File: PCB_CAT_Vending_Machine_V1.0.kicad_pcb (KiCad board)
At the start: 2 copper layers, 108 x 129 mm, 221 parts, among them J1 12Vin, J10 Load_0, J11 Load_1, J12 Load_2, J13 Load_3, J14 Load_4, J15 Load_5, J16 Load_6, J17 Load_07, J18 Screen, J19 Banknote, J2 Button_0, J20 QR ESP32, J21 Coin, J22 RASPI, J23 Water Level, J3 Button_1, J4 Button_2, J5 Button_3, J6 Button_4, J7 Button_5, J8 Button_6, J9 Button_7, Q1 2N7002, Q12 AO3400A, Q13 AO3400A, Q14 AO3400A, Q15 AO3400A, Q16 AO3400A, Q17 AO3400A, Q18 AO3400A, Q2 2N7002, Q3 AO3400A, Q4 2N7002, Q5 2N7002, Q6 2N7002, Q7 2N7002, Q8 2N7002, Q9 2N7002, SW1 Pairing, SW2 Add 10 BTH, U1 ESP32-S3-N16R8-Module, U10 PC817C-S, U11 PC817C-S, U12 PC817C-S, U13 PCA9557PW, U2 PCA9557PW, U3 PCA9557PW, U4 TPS5430DDA, U5 PC817C-S, U6 PC817C-S, U7 PC817C-S, U8 PC817C-S, U9 PC817C-S

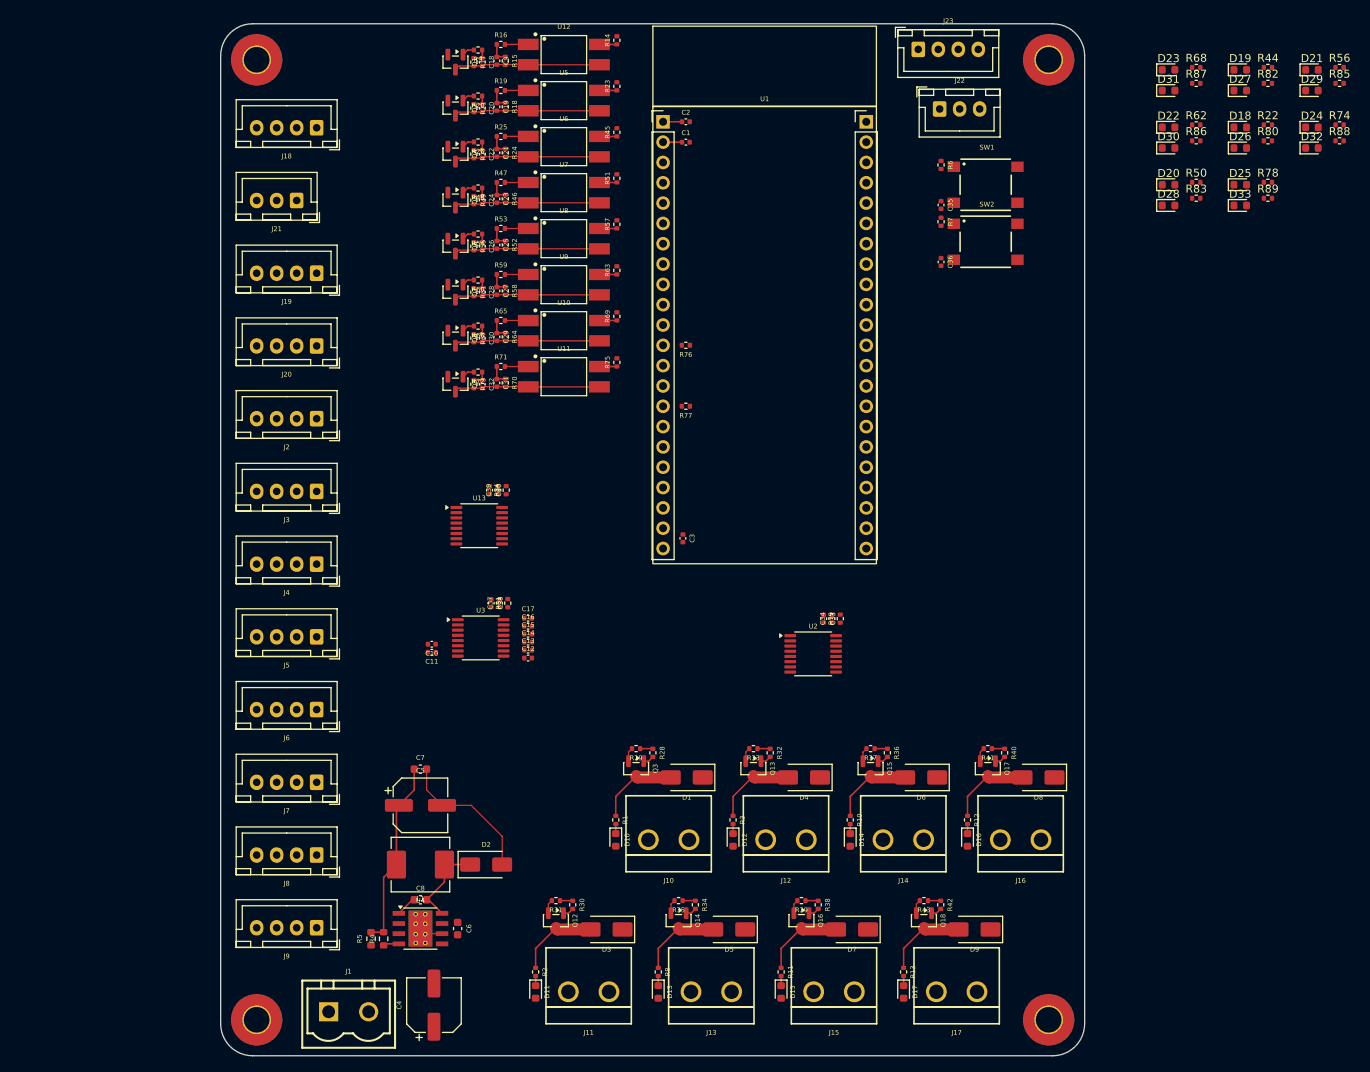
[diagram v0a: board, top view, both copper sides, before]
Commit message: PCB Connector Position
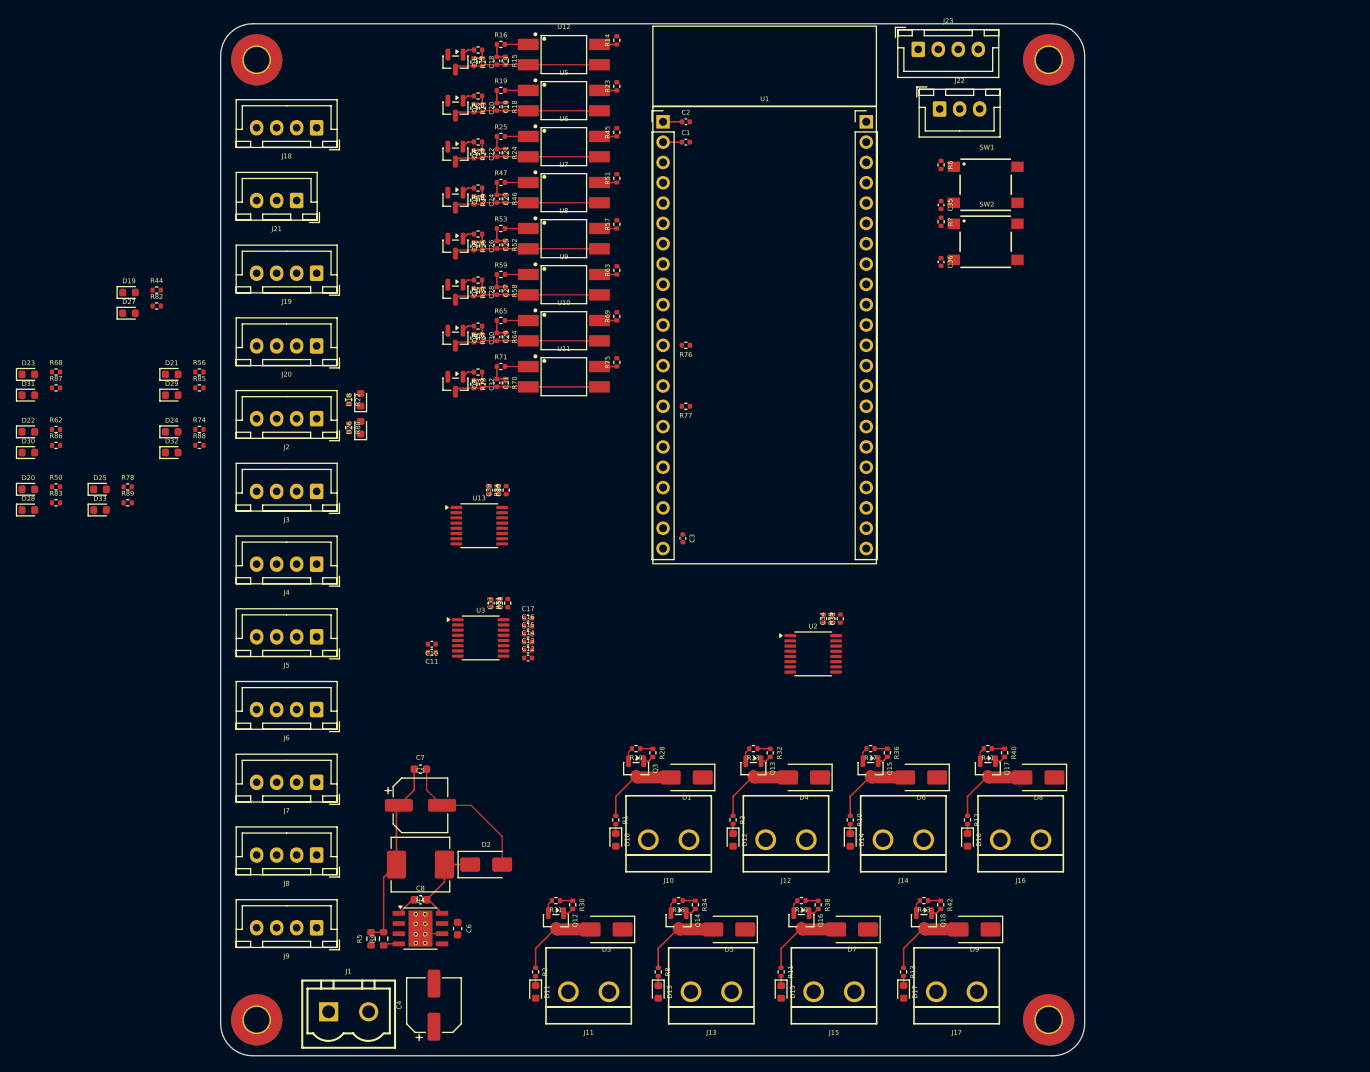
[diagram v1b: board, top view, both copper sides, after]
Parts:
- moved D20 147.5 mm to (-4.04, 78.2)
- moved D21 147.5 mm to (13.9, 63.8)
- moved D22 147.5 mm to (-4.04, 71.0)
- moved D23 147.5 mm to (-4.04, 63.8)
- moved D24 147.5 mm to (13.9, 71.0)
- moved D28 147.5 mm to (-4.04, 80.8)
- moved D29 147.5 mm to (13.9, 66.4)
- moved D30 147.5 mm to (-4.04, 73.6)
- moved D31 147.5 mm to (-4.04, 66.4)
- moved D32 147.5 mm to (13.9, 73.6)
- moved R56 147.5 mm to (17.3, 63.5)
- moved R74 147.5 mm to (17.3, 70.7)
- moved R78 147.5 mm to (8.38, 77.9)
- moved R85 147.5 mm to (17.3, 65.5)
- moved R88 147.5 mm to (17.3, 72.7)
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
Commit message: led
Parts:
- moved D27 39.2 mm to (39.5, 80.2), turned to 90 degrees
- moved D19 38.8 mm to (39.6, 76.9), turned to 90 degrees
- moved R82 35.2 mm to (36.9, 80.1), turned to -90 degrees
- moved R44 34.0 mm to (36.7, 76.6), turned to -90 degrees

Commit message: 3d
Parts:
- added J24: Water Level, Connector_JST:JST_XH_B4B-XH-A_1x04_P2.50mm_Vertical, F.Cu at (122.1, 56.9)
- added J25: Water Level, Connector_JST:JST_XH_B4B-XH-A_1x04_P2.50mm_Vertical, F.Cu at (122.1, 64.7)
- added J26: Water Level, Connector_JST:JST_XH_B4B-XH-A_1x04_P2.50mm_Vertical, F.Cu at (122.1, 72.5)
- added J27: Water Level, Connector_JST:JST_XH_B4B-XH-A_1x04_P2.50mm_Vertical, F.Cu at (122.1, 80.2)
- added J28: Water Level, Connector_JST:JST_XH_B4B-XH-A_1x04_P2.50mm_Vertical, F.Cu at (122.1, 88.0)
- moved R87 63.9 mm to (41.0, 114.0)
- moved D23 63.9 mm to (37.5, 112.3)
- moved D31 63.9 mm to (37.5, 114.9)
- moved R68 63.9 mm to (41.0, 112.0)
- moved D25 62.4 mm to (37.4, 131.5)
- moved D33 62.4 mm to (37.4, 134.1)
- moved R89 62.4 mm to (40.9, 133.2)
- moved R78 62.4 mm to (40.9, 131.2)
- moved R74 57.2 mm to (41.9, 122.4)
- moved D24 57.2 mm to (38.4, 122.7)
- moved D32 57.2 mm to (38.4, 125.3)
- moved R88 57.2 mm to (41.9, 124.4)
- moved D30 53.8 mm to (38.4, 106.6)
- moved R62 53.8 mm to (41.9, 103.7)
- moved D22 53.8 mm to (38.4, 104.0)
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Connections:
- net /Microcontroller/Water_Level.Echo renamed /Peripheral/Water_Trigger0
- J23 pad 1: +5V -> unconnected-(J23-Pin_1-Pad1)
- J23 pad 2: /Microcontroller/Water_Level.Trig -> GND
- J23 pad 4: GND -> +12V

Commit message: SCH finish
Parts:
- added C41: 100nF, Capacitor_SMD:C_0402_1005Metric, F.Cu at (95.4, 95.0)
- added C42: 100nF, Capacitor_SMD:C_0402_1005Metric, F.Cu at (94.4, 95.1)
- added C43: 1nF, Capacitor_SMD:C_0402_1005Metric, F.Cu at (71.9, 109.5)
- added C44: 1nF, Capacitor_SMD:C_0402_1005Metric, F.Cu at (61.9, 128.5)
- added C45: 1nF, Capacitor_SMD:C_0402_1005Metric, F.Cu at (86.6, 109.5)
- added C46: 1nF, Capacitor_SMD:C_0402_1005Metric, F.Cu at (77.2, 128.4)
- added C47: 1nF, Capacitor_SMD:C_0402_1005Metric, F.Cu at (101.2, 109.4)
- added C48: 1nF, Capacitor_SMD:C_0402_1005Metric, F.Cu at (92.6, 128.4)
- added C49: 1nF, Capacitor_SMD:C_0402_1005Metric, F.Cu at (115.9, 109.5)
- added C50: 1nF, Capacitor_SMD:C_0402_1005Metric, F.Cu at (107.9, 128.5)
- added J29: QR_Button, Connector_JST:JST_XH_B5B-XH-A_1x05_P2.50mm_Vertical, F.Cu at (42.1, 24.8)
- added Q10: PT15-21C/TR8, LED_SMD:LED_1206_3216Metric, F.Cu at (69.0, 95.6)
- added R90: 10k, Resistor_SMD:R_0402_1005Metric, F.Cu at (96.5, 95.0)
- added R91: 10k, Resistor_SMD:R_0402_1005Metric, F.Cu at (74.7, 95.8)
- added U14: PCA9557PW, Package_SO:TSSOP-16_4.4x5mm_P0.65mm, F.Cu at (92.2, 99.7)
- R1, R10, R11, R12, R13, R2, R22, R3, R44, R50, R56, R62, R68, R74, R78, R8, R80, R82, R83, R85, R86, R87, R88, R89: value 4.7k -> 3k
- moved J23 33.2 mm to (123.6, 52.1), turned to 180 degrees
- moved C36 14.5 mm to (108.3, 35.4)
- moved R7 14.5 mm to (108.3, 30.4)
- moved SW1 14.5 mm to (113.9, 25.8)
- moved SW2 14.5 mm to (113.9, 32.9)
- moved C35 14.5 mm to (108.3, 28.3)
- moved R6 14.5 mm to (108.3, 23.3)
- moved J22 14.4 mm to (118.6, 42.1)
- moved R79 11.1 mm to (86.4, 95.1)
- moved U2 11.1 mm to (83.0, 99.5)
- moved C33 11.1 mm to (84.4, 95.1)
- moved C34 11.1 mm to (85.4, 95.1)
- moved J28 8.71 mm to (123.6, 96.6)
- moved J27 7.62 mm to (123.6, 87.7)
- moved J26 6.53 mm to (123.6, 78.8)
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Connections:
- J23 pad 3: /Peripheral/Water_Trigger0 -> /Microcontroller/Water_Trigger0
- J24 pad 3: /Peripheral/Water_Trigger1 -> /Microcontroller/Water_Trigger1
- J25 pad 3: /Peripheral/Water_Trigger2 -> /Microcontroller/Water_Trigger2
- J26 pad 3: /Peripheral/Water_Trigger3 -> /Microcontroller/Water_Trigger3
- J27 pad 3: /Peripheral/Water_Trigger4 -> /Microcontroller/Water_Trigger4
- J28 pad 3: /Peripheral/Water_Trigger5 -> /Microcontroller/Water_Trigger5
- Q1 pad 2: /Connector/BTN0/GND_LED0 -> GND
- Q1 pad 3: GND -> /Connector/BTN0/GND_LED0
- Q2 pad 2: /Connector/BTN1/GND_LED1 -> GND
- Q2 pad 3: GND -> /Connector/BTN1/GND_LED1
- Q4 pad 2: /Connector/BTN2/GND_LED2 -> GND
- Q4 pad 3: GND -> /Connector/BTN2/GND_LED2
- Q5 pad 2: /Connector/BTN3/GND_LED3 -> GND
- Q5 pad 3: GND -> /Connector/BTN3/GND_LED3
- Q6 pad 2: /Connector/BTN4/GND_LED4 -> GND
- Q6 pad 3: GND -> /Connector/BTN4/GND_LED4
- Q7 pad 2: /Connector/BTN5/GND_LED5 -> GND
- Q7 pad 3: GND -> /Connector/BTN5/GND_LED5
- Q8 pad 2: /Connector/BTN6/GND_LED6 -> GND
- Q8 pad 3: GND -> /Connector/BTN6/GND_LED6
- Q9 pad 2: /Connector/BTN7/GND_LED7 -> GND
- Q9 pad 3: GND -> /Connector/BTN7/GND_LED7
- U1 pad 37: unconnected-(U1-GPIO40-Pad37) -> /Microcontroller/QR_Button0
- U1 pad 38: unconnected-(U1-GPIO41-Pad38) -> /Microcontroller/QR_Button1
- U1 pad 39: unconnected-(U1-GPIO42-Pad39) -> /Microcontroller/QR_Button2
- U1 pad 40: /Microcontroller/SW2 -> unconnected-(U1-GPIO2-Pad40)
- U1 pad 41: /Microcontroller/SW1 -> /Microcontroller/LightSen
- U3 pad 4: GND -> +3.3V
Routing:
- net GND: track 181.0 -> 152.7 mm

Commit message: finish no review
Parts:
- added C51: 10nF, Capacitor_SMD:C_0402_1005Metric, F.Cu at (105.0, 45.5)
- added C52: 10nF, Capacitor_SMD:C_0402_1005Metric, F.Cu at (105.0, 48.0)
- added C53: 10nF, Capacitor_SMD:C_0402_1005Metric, F.Cu at (105.0, 50.5)
- added J30: DoorSensor, Connector_JST:JST_XH_B2B-XH-A_1x02_P2.50mm_Vertical, F.Cu at (123.6, 33.0)
- added R92: 10k, Resistor_SMD:R_0402_1005Metric, F.Cu at (104.0, 45.5)
- added R93: 10k, Resistor_SMD:R_0402_1005Metric, F.Cu at (104.0, 48.0)
- added R94: 10k, Resistor_SMD:R_0402_1005Metric, F.Cu at (104.0, 50.5)
- added R95: 10k, Resistor_SMD:R_0402_1005Metric, F.Cu at (108.9, 51.5)
- added R96: 100, Resistor_SMD:R_0402_1005Metric, F.Cu at (104.5, 52.6)
- J29: footprint Connector_JST:JST_XH_B5B-XH-A_1x05_P2.50mm_Vertical -> Connector_JST:JST_XH_B4B-XH-A_1x04_P2.50mm_Vertical
- moved J29 83.3 mm to (123.6, 42.1)
- moved J22 76.2 mm to (44.5, 24.3), turned to 180 degrees
- moved SW1 75.0 mm to (100.3, 99.5), turned to -90 degrees
- moved R91 73.5 mm to (56.7, 24.5), turned to 180 degrees
- moved Q10 71.6 mm to (60.0, 24.5)
- moved R6 70.9 mm to (102.8, 94.0), turned to 180 degrees
- moved SW2 66.9 mm to (107.5, 99.5), turned to -90 degrees
- moved C35 66.5 mm to (97.8, 94.0), turned to 180 degrees
- moved R7 63.6 mm to (110.0, 94.0), turned to 180 degrees
- moved C36 58.6 mm to (105.0, 94.0), turned to 180 degrees
- moved C15 54.5 mm to (59.9, 41.9)
- moved C14 54.5 mm to (59.9, 42.8)
- moved C13 54.5 mm to (59.9, 43.8)
- moved C12 54.5 mm to (59.9, 44.8)
- moved C11 54.4 mm to (59.9, 45.8), turned to 0 degrees
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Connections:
- J1 pad 1: +12V -> GND
- J1 pad 2: GND -> +12V
- J18 pad 1: +3.3V -> /Microcontroller/Screen.CLK
- J18 pad 2: GND -> /Microcontroller/Screen.DIO
- J18 pad 3: /Microcontroller/Screen.DIO -> GND
- J18 pad 4: /Microcontroller/Screen.CLK -> +3.3V
- J19 pad 1: +12V -> GND
- J19 pad 2: GND -> /Microcontroller/Pulse
- J19 pad 3: /Microcontroller/Pulse -> GND
- J19 pad 4: GND -> +12V
- J20 pad 1: +5V -> GND
- J20 pad 4: GND -> +5V
- J21 pad 1: +12V -> GND
- J21 pad 3: GND -> +12V
- J29 pad 2: /Peripheral/QR_Button0 -> /Microcontroller/QR_Button0
- J29 pad 3: /Peripheral/QR_Button1 -> /Microcontroller/QR_Button1
- J29 pad 4: /Peripheral/QR_Button2 -> /Microcontroller/QR_Button2
- U1 pad 17: /Microcontroller/COIN -> /Microcontroller/Pulse
- U1 pad 18: /Microcontroller/Pulse -> /Microcontroller/COIN
- U1 pad 36: unconnected-(U1-GPIO39-Pad36) -> /Microcontroller/Door
- U13 pad 10: /Connector/LED3 -> /Connector/LED4
- U13 pad 11: /Connector/LED4 -> /Connector/LED3
- U13 pad 12: /Connector/LED5 -> /Connector/LED2
- U13 pad 13: /Connector/LED6 -> /Connector/LED1
- U13 pad 14: /Connector/LED7 -> /Connector/LED0
- U13 pad 6: /Connector/LED0 -> /Connector/LED7
- U13 pad 7: /Connector/LED1 -> /Connector/LED6
- U13 pad 9: /Connector/LED2 -> /Connector/LED5
- U14 pad 10: /Microcontroller/Water_Trigger3 -> /Microcontroller/Water_Trigger2
- U14 pad 11: /Microcontroller/Water_Trigger4 -> /Microcontroller/Water_Trigger1
- U14 pad 12: /Microcontroller/Water_Trigger5 -> /Microcontroller/Water_Trigger0
- U14 pad 6: /Microcontroller/Water_Trigger0 -> /Microcontroller/Water_Trigger4
- U14 pad 7: /Microcontroller/Water_Trigger1 -> /Microcontroller/Water_Trigger5
- U14 pad 9: /Microcontroller/Water_Trigger2 -> /Microcontroller/Water_Trigger3
- U2 pad 10: /Connector/LD3 -> /Connector/LD2
- U2 pad 11: /Connector/LD4 -> /Connector/LD5
- U2 pad 12: /Connector/LD5 -> /Connector/LD4
- U2 pad 13: /Connector/LD6 -> /Connector/LD7
- U2 pad 14: /Connector/LD7 -> /Connector/LD6
- U2 pad 9: /Connector/LD2 -> /Connector/LD3
- U3 pad 10: /Connector/BTN3 -> /Connector/BTN1
- U3 pad 11: /Connector/BTN4 -> /Connector/BTN2
- U3 pad 12: /Connector/BTN5 -> /Connector/BTN3
- U3 pad 13: /Connector/BTN6 -> /Connector/BTN4
- U3 pad 14: /Connector/BTN7 -> /Connector/BTN5
- U3 pad 6: /Connector/BTN0 -> /Connector/BTN7
- U3 pad 7: /Connector/BTN1 -> /Connector/BTN6
- U3 pad 9: /Connector/BTN2 -> /Connector/BTN0
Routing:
- net +12V: track 0.00 -> 1004.4 mm, vias 0 -> 49
- net +3.3V: track 4.74 -> 603.1 mm, vias 0 -> 23
- net /Microcontroller/I2C_SDA: track 0.00 -> 206.0 mm, vias 0 -> 3
- net /Microcontroller/I2C_SCL: track 0.00 -> 202.1 mm, vias 0 -> 3
- net +5V: track 23.5 -> 197.8 mm, vias 0 -> 9
- net /Microcontroller/RASPI.RX: track 0.00 -> 137.5 mm
- net /Microcontroller/RASPI.TX: track 0.00 -> 136.8 mm
- net GND: track 152.7 -> 289.0 mm, vias 0 -> 324
- net /Microcontroller/COIN: track 0.00 -> 100.0 mm
- net /Connector/LED7: track 2.12 -> 91.1 mm, vias 0 -> 2
- net /Microcontroller/Pulse: track 0.00 -> 88.2 mm
- net /Connector/LED5: track 2.12 -> 84.5 mm, vias 0 -> 2
- net /Connector/LED6: track 2.12 -> 83.0 mm, vias 0 -> 2
- net /Connector/LED4: track 2.12 -> 77.9 mm, vias 0 -> 2
- net /Connector/LED3: track 2.12 -> 71.4 mm, vias 0 -> 2
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- added copper zone on B.Cu, net +12V
- added copper zone on F.Cu, net +12V
- added copper zone on F.Cu, net +5V
- added copper zone on B.Cu, net GND
- added copper zone on F.Cu, net GND
- added copper zone on F.Cu, net Net-(D2-K)

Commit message: success
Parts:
- removed R80, R82, R83, R85, R86, R87, R88, R89: 3k, Resistor_SMD:R_0402_1005Metric
- added C54: 10nF, Capacitor_SMD:C_0402_1005Metric, F.Cu at (104.5, 39.9)
- added C55: 100nF, Capacitor_SMD:C_0402_1005Metric, F.Cu at (105.0, 53.0)
- added C57: 10nF, Capacitor_SMD:C_0402_1005Metric, F.Cu at (91.6, 99.5)
- added C58: 10nF, Capacitor_SMD:C_0402_1005Metric, F.Cu at (91.6, 101.3)
- added C59: 10nF, Capacitor_SMD:C_0402_1005Metric, F.Cu at (90.5, 91.3)
- added C60: 10nF, Capacitor_SMD:C_0402_1005Metric, F.Cu at (88.6, 91.3)
- added C61: 10nF, Capacitor_SMD:C_0402_1005Metric, F.Cu at (86.7, 91.3)
- added C62: 10nF, Capacitor_SMD:C_0402_1005Metric, F.Cu at (84.8, 91.3)
- added JP1: Bankenote Selector, Jumper:SolderJumper-3_P1.3mm_Open_RoundedPad1.0x1.5mm, F.Cu at (65.0, 39.0)
- added R100: 10k, Resistor_SMD:R_0402_1005Metric, F.Cu at (90.5, 90.3)
- added R101: 10k, Resistor_SMD:R_0402_1005Metric, F.Cu at (88.6, 90.3)
- added R102: 10k, Resistor_SMD:R_0402_1005Metric, F.Cu at (86.7, 90.3)
- added R103: 10k, Resistor_SMD:R_0402_1005Metric, F.Cu at (84.8, 90.3)
- added R104: 27k, Resistor_SMD:R_0603_1608Metric, F.Cu at (117.8, 91.5)
- added R105: 27k, Resistor_SMD:R_0603_1608Metric, F.Cu at (117.8, 100.4)
- added R106: 27k, Resistor_SMD:R_0603_1608Metric, F.Cu at (117.8, 82.6)
- added R107: 27k, Resistor_SMD:R_0603_1608Metric, F.Cu at (117.8, 73.7)
- added R108: 27k, Resistor_SMD:R_0603_1608Metric, F.Cu at (117.8, 64.8)
- added R109: 27k, Resistor_SMD:R_0603_1608Metric, F.Cu at (117.8, 55.9)
- added R110: 220, Resistor_SMD:R_0402_1005Metric, F.Cu at (90.2, 100.9)
- added R111: 220, Resistor_SMD:R_0402_1005Metric, F.Cu at (89.2, 93.4)
- added R112: 220, Resistor_SMD:R_0402_1005Metric, F.Cu at (88.2, 93.4)
- added R113: 220, Resistor_SMD:R_0402_1005Metric, F.Cu at (87.1, 93.4)
- added R114: 220, Resistor_SMD:R_0402_1005Metric, F.Cu at (86.1, 93.4)
- added R115: 4.7k, Resistor_SMD:R_0402_1005Metric, F.Cu at (78.2, 39.9)
- added R116: 4.7k, Resistor_SMD:R_0402_1005Metric, F.Cu at (78.2, 42.4)
- added R117: 10k, Resistor_SMD:R_0402_1005Metric, F.Cu at (69.5, 107.8)
- added R118: 10k, Resistor_SMD:R_0402_1005Metric, F.Cu at (85.9, 107.8)
- added R119: 10k, Resistor_SMD:R_0402_1005Metric, F.Cu at (81.5, 108.5)
- added R120: 10k, Resistor_SMD:R_0402_1005Metric, F.Cu at (99.3, 106.5)
- added R121: 10k, Resistor_SMD:R_0402_1005Metric, F.Cu at (94.8, 107.2)
- added R122: 10k, Resistor_SMD:R_0402_1005Metric, F.Cu at (82.5, 104.7)
- added R123: 4.7k, Resistor_SMD:R_0402_1005Metric, F.Cu at (78.2, 75.5)
- added R124: 10k, Resistor_SMD:R_0402_1005Metric, F.Cu at (101.8, 106.4)
- added R97: 220, Resistor_SMD:R_0402_1005Metric, F.Cu at (90.2, 99.9)
- added R98: 10k, Resistor_SMD:R_0402_1005Metric, F.Cu at (92.6, 99.5)
- added R99: 10k, Resistor_SMD:R_0402_1005Metric, F.Cu at (92.6, 101.3)
- C18, C20, C22, C24, C26, C28, C30, C32, C43, C44, C45, C46, C47, C48, C49, C50: value 1nF -> 10nF
- C51, C52, C53: value 10nF -> 100nF
- J10: value Load_0 -> Load
- J11: value Load_1 -> Load
- J12: value Load_2 -> Load
- J13: value Load_3 -> Load
- J14: value Load_4 -> Load
- J15: value Load_5 -> Load
- J16: value Load_6 -> Load
- J17: value Load_07 -> Load
- J18: value Screen -> Connector 4P
- J19: value Banknote -> Connector 4P
- J2: value Button_0 -> Connector 4P
- J20: value QR ESP32 -> Connector 4P
- J21: value Coin -> Connector 3P
- J22: value RASPI -> Connector 3P
- J23, J24, J25, J26, J27, J28: value Water Level -> Connector 4P
- J29: value QR_Button -> Connector 4P
- J3: value Button_1 -> Connector 4P
- J30: value DoorSensor -> Connector2P
- J4: value Button_2 -> Connector 4P
- J5: value Button_3 -> Connector 4P
- J6: value Button_4 -> Connector 4P
- J7: value Button_5 -> Connector 4P
- J8: value Button_6 -> Connector 4P
- J9: value Button_7 -> Connector 4P
- R1, R10, R11, R12, R13, R2, R22, R3, R44, R50, R56, R62, R68, R74, R78, R8: value 3k -> 1k
- R17, R21, R27, R49, R55, R61, R67, R73: value 100k -> 10k
- R29, R31, R33, R35, R37, R39, R41, R43: value 100k -> 1k
- R96: value 100 -> 10k
- moved R41 81.2 mm to (36.0, 125.0), turned to -90 degrees
- moved R43 72.1 mm to (36.0, 134.1), turned to -90 degrees
- moved R37 65.3 mm to (36.0, 106.9), turned to -90 degrees
- moved R96 64.9 mm to (75.6, 110.6)
- moved R39 58.2 mm to (36.0, 116.0), turned to -90 degrees
- moved R31 56.3 mm to (36.0, 79.6), turned to -90 degrees
- moved R33 55.1 mm to (36.0, 88.7), turned to -90 degrees
- moved R29 53.8 mm to (36.0, 70.5), turned to -90 degrees
- moved R35 52.1 mm to (36.0, 97.8), turned to -90 degrees
- moved R91 43.6 mm to (97.8, 39.1), turned to -90 degrees
- moved R95 11.2 mm to (97.8, 52.5), turned to 0 degrees
- moved R92 6.27 mm to (97.8, 45.0), turned to 0 degrees
- moved R93 6.27 mm to (97.8, 47.5), turned to 0 degrees
- moved R94 6.27 mm to (97.8, 50.0), turned to 0 degrees
- moved C41 5.66 mm to (83.0, 99.2)
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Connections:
- J10 pad 1: +12V -> /Connector/Load0/GND_Load0
- J10 pad 2: /Connector/Load0/GND_Load0 -> +12V
- J11 pad 1: +12V -> /Connector/Load1/GND_Load1
- J11 pad 2: /Connector/Load1/GND_Load1 -> +12V
- J12 pad 1: +12V -> /Connector/Load2/GND_Load2
- J12 pad 2: /Connector/Load2/GND_Load2 -> +12V
- J13 pad 1: +12V -> /Connector/Load3/GND_Load3
- J13 pad 2: /Connector/Load3/GND_Load3 -> +12V
- J14 pad 1: +12V -> /Connector/Load4/GND_Load4
- J14 pad 2: /Connector/Load4/GND_Load4 -> +12V
- J15 pad 1: +12V -> /Connector/Load5/GND_Load5
- J15 pad 2: /Connector/Load5/GND_Load5 -> +12V
- J16 pad 1: +12V -> /Connector/Load6/GND_Load6
- J16 pad 2: /Connector/Load6/GND_Load6 -> +12V
- J17 pad 1: +12V -> /Connector/Load7/GND_Load7
- J17 pad 2: /Connector/Load7/GND_Load7 -> +12V
- J18 pad 4: +3.3V -> +5V
- J19 pad 2: /Microcontroller/Pulse -> /Microcontroller/Bank_RX
- J19 pad 3: GND -> Net-(J19-Pin_3)
- J2 pad 1: +12V -> /Connector/BTN0/12V_BTN0
- J2 pad 2: /Connector/BTN0/GND_LED0 -> +12V
- J2 pad 3: +12V -> /Connector/BTN0/GND_LED0
- J2 pad 4: /Connector/BTN0/12V_BTN0 -> +12V
- J23 pad 1: unconnected-(J23-Pin_1-Pad1) -> +12V
- J23 pad 2: GND -> /Microcontroller/Water_Trigger0
- J23 pad 3: /Microcontroller/Water_Trigger0 -> GND
- J23 pad 4: +12V -> unconnected-(J23-Pin_4-Pad4)
- J24 pad 1: unconnected-(J24-Pin_1-Pad1) -> +12V
- J24 pad 2: GND -> /Microcontroller/Water_Trigger1
- J24 pad 3: /Microcontroller/Water_Trigger1 -> GND
- J24 pad 4: +12V -> unconnected-(J24-Pin_4-Pad4)
- J25 pad 1: unconnected-(J25-Pin_1-Pad1) -> +12V
- J25 pad 2: GND -> /Microcontroller/Water_Trigger2
- J25 pad 3: /Microcontroller/Water_Trigger2 -> GND
- J25 pad 4: +12V -> unconnected-(J25-Pin_4-Pad4)
- J26 pad 1: unconnected-(J26-Pin_1-Pad1) -> +12V
- J26 pad 2: GND -> /Microcontroller/Water_Trigger3
- J26 pad 3: /Microcontroller/Water_Trigger3 -> GND
- J26 pad 4: +12V -> unconnected-(J26-Pin_4-Pad4)
- J27 pad 1: unconnected-(J27-Pin_1-Pad1) -> +12V
- J27 pad 2: GND -> /Microcontroller/Water_Trigger4
- J27 pad 3: /Microcontroller/Water_Trigger4 -> GND
- J27 pad 4: +12V -> unconnected-(J27-Pin_4-Pad4)
- J28 pad 1: unconnected-(J28-Pin_1-Pad1) -> +12V
- J28 pad 2: GND -> /Microcontroller/Water_Trigger5
- J28 pad 3: /Microcontroller/Water_Trigger5 -> GND
- J28 pad 4: +12V -> unconnected-(J28-Pin_4-Pad4)
- J29 pad 1: +3.3V -> GND
- J3 pad 1: +12V -> /Connector/BTN1/12V_BTN1
- J3 pad 2: /Connector/BTN1/GND_LED1 -> +12V
- J3 pad 3: +12V -> /Connector/BTN1/GND_LED1
- J3 pad 4: /Connector/BTN1/12V_BTN1 -> +12V
- J30 pad 1: Net-(J30-Pin_1) -> /Microcontroller/Door
- J4 pad 1: +12V -> /Connector/BTN2/12V_BTN2
- J4 pad 2: /Connector/BTN2/GND_LED2 -> +12V
- J4 pad 3: +12V -> /Connector/BTN2/GND_LED2
- J4 pad 4: /Connector/BTN2/12V_BTN2 -> +12V
- J5 pad 1: +12V -> /Connector/BTN3/12V_BTN3
- J5 pad 2: /Connector/BTN3/GND_LED3 -> +12V
- J5 pad 3: +12V -> /Connector/BTN3/GND_LED3
- J5 pad 4: /Connector/BTN3/12V_BTN3 -> +12V
- J6 pad 1: +12V -> /Connector/BTN4/12V_BTN4
- J6 pad 2: /Connector/BTN4/GND_LED4 -> +12V
- J6 pad 3: +12V -> /Connector/BTN4/GND_LED4
- J6 pad 4: /Connector/BTN4/12V_BTN4 -> +12V
- J7 pad 1: +12V -> /Connector/BTN5/12V_BTN5
- J7 pad 2: /Connector/BTN5/GND_LED5 -> +12V
- J7 pad 3: +12V -> /Connector/BTN5/GND_LED5
- J7 pad 4: /Connector/BTN5/12V_BTN5 -> +12V
- J8 pad 1: +12V -> /Connector/BTN6/12V_BTN6
- J8 pad 2: /Connector/BTN6/GND_LED6 -> +12V
- J8 pad 3: +12V -> /Connector/BTN6/GND_LED6
- J8 pad 4: /Connector/BTN6/12V_BTN6 -> +12V
- J9 pad 1: +12V -> /Connector/BTN7/12V_BTN7
- J9 pad 2: /Connector/BTN7/GND_LED7 -> +12V
- J9 pad 3: +12V -> /Connector/BTN7/GND_LED7
- J9 pad 4: /Connector/BTN7/12V_BTN7 -> +12V
- R17 pad 1: /Connector/LED0 -> +3.3V
- R17 pad 2: GND -> /Connector/LED0
- R21 pad 1: /Connector/LED1 -> +3.3V
- R21 pad 2: GND -> /Connector/LED1
- R27 pad 1: /Connector/LED2 -> +3.3V
- R27 pad 2: GND -> /Connector/LED2
- R29 pad 1: /Connector/LD0 -> /Connector/BTN0/GND_LED0
- R29 pad 2: GND -> Net-(D26-K)
- R31 pad 1: /Connector/LD1 -> /Connector/BTN1/GND_LED1
- R31 pad 2: GND -> Net-(D27-K)
- R33 pad 1: /Connector/LD2 -> /Connector/BTN2/GND_LED2
- R33 pad 2: GND -> Net-(D28-K)
- R35 pad 1: /Connector/LD3 -> /Connector/BTN3/GND_LED3
- R35 pad 2: GND -> Net-(D29-K)
- R37 pad 1: /Connector/LD4 -> /Connector/BTN4/GND_LED4
- R37 pad 2: GND -> Net-(D30-K)
- R39 pad 1: /Connector/LD5 -> /Connector/BTN5/GND_LED5
- R39 pad 2: GND -> Net-(D31-K)
- R41 pad 1: /Connector/LD6 -> /Connector/BTN6/GND_LED6
- R41 pad 2: GND -> Net-(D32-K)
- R43 pad 1: /Connector/LD7 -> /Connector/BTN7/GND_LED7
- R43 pad 2: GND -> Net-(D33-K)
- R49 pad 1: /Connector/LED3 -> +3.3V
- R49 pad 2: GND -> /Connector/LED3
- R55 pad 1: /Connector/LED4 -> +3.3V
- R55 pad 2: GND -> /Connector/LED4
- R61 pad 1: /Connector/LED5 -> +3.3V
- R61 pad 2: GND -> /Connector/LED5
- R67 pad 1: /Connector/LED6 -> +3.3V
- R67 pad 2: GND -> /Connector/LED6
- R73 pad 1: /Connector/LED7 -> +3.3V
- R73 pad 2: GND -> /Connector/LED7
- R92 pad 1: GND -> +3.3V
- R93 pad 1: GND -> +3.3V
- R94 pad 1: GND -> +3.3V
- R96 pad 1: Net-(J30-Pin_1) -> +3.3V
- R96 pad 2: /Microcontroller/Door -> /Connector/LD0
- U1 pad 17: /Microcontroller/Pulse -> unconnected-(U1-GPIO11-Pad17)
- U1 pad 4: unconnected-(U1-GPIO4-Pad4) -> /Microcontroller/Pulse/Bank_TX
- U1 pad 5: unconnected-(U1-GPIO5-Pad5) -> /Microcontroller/Bank_RX
- U14 pad 10: /Microcontroller/Water_Trigger2 -> Net-(U14-IO3)
- U14 pad 11: /Microcontroller/Water_Trigger1 -> Net-(U14-IO4)
- U14 pad 12: /Microcontroller/Water_Trigger0 -> Net-(U14-IO5)
- U14 pad 6: /Microcontroller/Water_Trigger4 -> Net-(U14-IO0)
- U14 pad 7: /Microcontroller/Water_Trigger5 -> Net-(U14-IO1)
- U14 pad 9: /Microcontroller/Water_Trigger3 -> Net-(U14-IO2)
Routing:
- net +12V: track 1004.4 -> 816.7 mm
- net /Microcontroller/Bank_RX: track 0.00 -> 90.2 mm
- net /Microcontroller/Pulse: track 88.2 -> 0.00 mm
- net Net-(J19-Pin_3): track 0.00 -> 75.0 mm
- net /Microcontroller/Water_Divider 0: track 0.00 -> 63.9 mm
- net /Microcontroller/Water_Trigger0: track 60.4 -> 4.83 mm
- net /Microcontroller/Water_Divider 1: track 0.00 -> 54.5 mm
- net /Microcontroller/Water_Trigger1: track 51.3 -> 4.82 mm
- net /Microcontroller/Water_Divider 2: track 0.00 -> 43.1 mm
- net /Microcontroller/Water_Trigger2: track 42.2 -> 4.81 mm
- net +3.3V: track 603.1 -> 638.5 mm, vias 23 -> 37
- net Net-(J30-Pin_1): track 35.0 -> 0.00 mm
- net /Microcontroller/Door: track 8.13 -> 41.9 mm
- net /Microcontroller/Water_Divider 3: track 0.00 -> 33.7 mm
- net /Microcontroller/Water_Divider 4: track 0.00 -> 29.8 mm
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- added copper zone on F.Cu, net Net-(U4-BOOT)
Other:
- board text added: "12V"
- board text added: "<->"
- board text added: "BTN0"
- board text added: "BTN1"
- board text added: "BTN2"
- board text added: "BTN3"
- board text added: "BTN4"
- board text added: "BTN5"
- board text added: "BTN6"
- board text added: "BTN7"
- board text added: "Banknote"
- board text added: "CH0"
- board text added: "CH1"
- board text added: "CH2"
- board text added: "CH3"
- board text added: "CH4"
- board text added: "CH5"
- board text added: "CH6"
- board text added: "CH7"
- board text added: "Coin"
- board text added: "Door"
- board text added: "ESP32-S3"
- board text added: "GND"
- board text added: "Mode selector"
- board text added: "Pulse"
- board text added: "QR ESP32"
- board text added: "QR_Button"
- board text added: "RPi"
- board text added: "SSP"
- board text added: "Screen"
- board text added: "Water0"
- board text added: "Water1"
- board text added: "Water2"
- board text added: "Water3"
- board text added: "Water4"
- board text added: "Water5"
